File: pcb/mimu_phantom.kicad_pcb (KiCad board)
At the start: 2 copper layers, 0 parts

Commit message: I hope this did not break everything
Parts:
- added C1: 0.1uF, Capacitor_SMD:C_0805_2012Metric_Pad1.15x1.40mm_HandSolder, F.Cu at (148.8, 97.5)
- added C2: 0.1uF, Capacitor_SMD:C_0805_2012Metric_Pad1.15x1.40mm_HandSolder, F.Cu at (148.8, 100.5)
- added C3: 1uF, Capacitor_THT:C_Rect_L7.0mm_W3.5mm_P2.50mm_P5.00mm, F.Cu at (186.1, 112.7)
- added C4: 1uF, Capacitor_THT:C_Rect_L7.0mm_W3.5mm_P2.50mm_P5.00mm, F.Cu at (186.1, 117.8)
- added C_B1: 100nF, Capacitor_SMD:C_1206_3216Metric_Pad1.42x1.75mm_HandSolder, F.Cu at (181.3, 101.2)
- added C_IN1: 10uF, Capacitor_SMD:C_1206_3216Metric_Pad1.42x1.75mm_HandSolder, F.Cu at (182.7, 96.9)
- added C_IN2: 10uF, Capacitor_SMD:C_1206_3216Metric_Pad1.42x1.75mm_HandSolder, F.Cu at (190.8, 92.3)
- added C_out1: 10uF, Capacitor_SMD:C_1206_3216Metric_Pad1.42x1.75mm_HandSolder, F.Cu at (188.7, 96.9)
- added C_out2: 10uF, Capacitor_SMD:C_1206_3216Metric_Pad1.42x1.75mm_HandSolder, F.Cu at (187.2, 100.2)
- added D1: B1100, Diode_SMD:D_SMA, F.Cu at (174.3, 101.8)
- added D_B1: 1N4148, Diode_SMD:D_SMA, F.Cu at (183.8, 93.0)
- added D_LED1: LED, LED_THT:LED_D3.0mm, F.Cu at (142.2, 98.8)
- added INPUT1: XLR3, Connector_PinHeader_2.54mm:PinHeader_1x03_P2.54mm_Vertical, F.Cu at (155.4, 82.0)
- added ISP1: AVR-ISP-6, Connector_PinHeader_2.54mm:PinHeader_2x03_P2.54mm_Vertical, F.Cu at (160.1, 82.0)
- added J1: OPT, Connector_PinHeader_1.27mm:PinHeader_1x05_P1.27mm_Vertical, F.Cu at (158.0, 91.1)
- added L1: 15uH, Inductor_SMD:L_7.3x7.3_H4.5, F.Cu at (175.0, 95.1)
- added OUTPUT1: XLR3, Connector_PinHeader_2.54mm:PinHeader_1x03_P2.54mm_Vertical, F.Cu at (153.6, 92.8)
- added R1: 165R, Resistor_SMD:R_1206_3216Metric_Pad1.42x1.75mm_HandSolder, F.Cu at (143.8, 88.5)
- added R2: 110R, Resistor_SMD:R_1206_3216Metric_Pad1.42x1.75mm_HandSolder, F.Cu at (142.1, 94.0)
- added RV1: 1K_POT, Potentiometer_THT:Potentiometer_Bourns_PTV09A-2_Single_Horizontal, F.Cu at (161.4, 116.3)
- added R_1: 10, Resistor_SMD:R_1206_3216Metric_Pad1.42x1.75mm_HandSolder, F.Cu at (189.1, 79.4)
- added R_BOT1: 10k, Resistor_SMD:R_1206_3216Metric_Pad1.42x1.75mm_HandSolder, F.Cu at (189.1, 82.7)
- added R_TOP1: 31.2k, Resistor_SMD:R_1206_3216Metric_Pad1.42x1.75mm_HandSolder, F.Cu at (195.1, 79.4)
- added SENS1: Sens, Connector_PinHeader_2.54mm:PinHeader_1x04_P2.54mm_Horizontal, F.Cu at (131.2, 82.0)
- added SW2: SW_DPDT_x2, Jumper:SolderJumper-3_P1.3mm_Bridged12_RoundedPad1.0x1.5mm, F.Cu at (167.8, 81.5)
- added U1: AQY211EH, custom:DIP-4_bubble_W7.62mm, F.Cu at (143.9, 81.8)
- added U2: ATTINY88AU, Package_QFP:TQFP-32_7x7mm_P0.8mm, F.Cu at (134.7, 97.8)
- added U3: MCP16331CH, Package_TO_SOT_SMD:SOT-23-6, F.Cu at (178.1, 82.0)

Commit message: Quick layout test
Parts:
- removed R_1: 10, Resistor_SMD:R_1206_3216Metric_Pad1.42x1.75mm_HandSolder
- added R3: 6.8Ohm 0.1%, Resistor_SMD:R_1206_3216Metric_Pad1.42x1.75mm_HandSolder, F.Cu at (131.4, 88.2)
- added R4: 6.8Ohm 0.1%, Resistor_SMD:R_1206_3216Metric_Pad1.42x1.75mm_HandSolder, F.Cu at (134.0, 88.2)
- moved R_TOP1 90.3 mm to (106.0, 94.2), turned to 90 degrees
- moved R_BOT1 83.4 mm to (106.0, 89.2), turned to 90 degrees
- moved C_out1 80.3 mm to (108.4, 94.3), turned to 90 degrees
- moved C_out2 72.9 mm to (114.6, 94.3), turned to 90 degrees
- moved D_B1 72.3 mm to (111.5, 93.2), turned to 270 degrees
- moved C4 70.3 mm to (129.4, 76.2)
- moved RV1 65.8 mm to (110.4, 74.7), turned to 90 degrees
- moved C3 65.4 mm to (129.4, 80.2)
- moved U3 60.5 mm to (119.0, 94.9)
- moved C_B1 58.1 mm to (123.7, 94.2), turned to 180 degrees
- moved C_IN2 54.4 mm to (136.4, 91.2), turned to 270 degrees
- moved L1 53.6 mm to (121.8, 89.0)
- moved C_IN1 50.2 mm to (132.7, 92.6)
- moved D1 49.8 mm to (124.7, 97.4), turned to 180 degrees
- moved SW2 41.5 mm to (126.4, 78.4), turned to 90 degrees
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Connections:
- net Net-(C3-Pad1) renamed XLR_HOT
- net Net-(INPUT1-Pad3) renamed XLR_COLD
- C1 pad 2: GND -> XLR_GND
- C2 pad 2: GND -> XLR_GND
- C_IN1 pad 2: GND -> XLR_GND
- C_IN2 pad 2: GND -> XLR_GND
- C_out1 pad 2: GND -> XLR_GND
- C_out2 pad 2: GND -> XLR_GND
- D1 pad 2: GND -> XLR_GND
- D_LED1 pad 1: GND -> XLR_GND
- INPUT1 pad 1: Net-(INPUT1-Pad1) -> XLR_GND
- ISP1 pad 6: GND -> XLR_GND
- J1 pad 4: GND -> XLR_GND
- OUTPUT1 pad 1: Net-(INPUT1-Pad1) -> XLR_GND
- RV1 pad 1: GND -> XLR_GND
- R_BOT1 pad 2: GND -> XLR_GND
- R_TOP1 pad 1: Net-(R_1-Pad2) -> VCC
- SENS1 pad 2: GND -> XLR_GND
- U1 pad 2: GND -> XLR_GND
- U2 pad 21: GND -> XLR_GND
- U2 pad 5: GND -> XLR_GND
- U3 pad 2: GND -> XLR_GND
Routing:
- net XLR_GND: track 0.00 -> 159.9 mm, vias 0 -> 3
- net VCC: track 0.00 -> 135.8 mm, vias 0 -> 4
- net POT: track 0.00 -> 44.1 mm
- net XLR_COLD: track 0.00 -> 31.7 mm
- net XLR_HOT: track 0.00 -> 25.2 mm
- net Net-(C_B1-Pad1): track 0.00 -> 25.0 mm, vias 0 -> 2
- net Net-(R2-Pad2): track 0.00 -> 24.5 mm, vias 0 -> 1
- net Net-(ISP1-Pad5): track 0.00 -> 24.1 mm, vias 0 -> 2
- net Net-(J1-Pad3): track 0.00 -> 22.2 mm, vias 0 -> 2
- net +BATT: track 0.00 -> 21.1 mm, vias 0 -> 2
- net LED: track 0.00 -> 20.5 mm, vias 0 -> 2
- net Net-(J1-Pad2): track 0.00 -> 19.8 mm, vias 0 -> 2
- net Net-(R_BOT1-Pad1): track 0.00 -> 15.8 mm, vias 0 -> 2
- net Net-(J1-Pad1): track 0.00 -> 15.3 mm, vias 0 -> 1
- net SCL: track 0.00 -> 14.4 mm, vias 0 -> 1
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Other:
- board outline added: 60 x 30 mm

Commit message: Now it just has to work, lol
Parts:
- added TP1: TestPoint, Measurement_Points:Measurement_Point_Round-SMD-Pad_Small, F.Cu at (128.8, 89.8)
- added TP3: TestPoint, Measurement_Points:Measurement_Point_Round-SMD-Pad_Small, F.Cu at (103.0, 97.5)
- added TP4: TestPoint, Measurement_Points:Measurement_Point_Round-SMD-Pad_Small, F.Cu at (106.0, 85.2)
- added TP5: TestPoint, Measurement_Points:Measurement_Point_Round-SMD-Pad_Small, F.Cu at (141.0, 71.5)
- moved R3 0.31 mm to (131.4, 88.5)
- moved R4 0.30 mm to (134.0, 88.5)
- moved OUTPUT1 0.30 mm to (129.0, 72.2)
- moved D_LED1 0.10 mm to (157.4, 96.0)
- renumbered C_out1 to Cout1, C_out2 to Cout2
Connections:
- ISP1 pad 2: (no net) -> +3V0
- U2 pad 1: (no net) -> Net-(U2-Pad1)
- U2 pad 10: (no net) -> Net-(U2-Pad10)
- U2 pad 11: (no net) -> Net-(U2-Pad11)
- U2 pad 12: (no net) -> Net-(U2-Pad12)
- U2 pad 13: (no net) -> Net-(U2-Pad13)
- U2 pad 14: (no net) -> Net-(U2-Pad14)
- U2 pad 19: (no net) -> Net-(U2-Pad19)
- U2 pad 2: (no net) -> Net-(U2-Pad2)
- U2 pad 20: (no net) -> Net-(U2-Pad20)
- U2 pad 22: (no net) -> Net-(U2-Pad22)
- U2 pad 26: (no net) -> Net-(U2-Pad26)
- U2 pad 3: (no net) -> Net-(U2-Pad3)
- U2 pad 6: (no net) -> Net-(U2-Pad6)
- U2 pad 7: (no net) -> Net-(U2-Pad7)
- U2 pad 8: (no net) -> Net-(U2-Pad8)
- U2 pad 9: (no net) -> Net-(U2-Pad9)
- U3 pad 4: (no net) -> Net-(U3-Pad4)
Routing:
- net XLR_GND: track 159.9 -> 132.7 mm, vias 3 -> 8
- net VCC: track 135.8 -> 160.9 mm
- net Net-(R_BOT1-Pad1): track 15.8 -> 23.1 mm
- net +BATT: track 21.1 -> 23.9 mm
- net XLR_HOT: track 25.2 -> 27.7 mm
- net Net-(C3-Pad2): track 14.2 -> 16.7 mm
- net POT: track 44.1 -> 46.3 mm
- net SDA: track 14.2 -> 16.0 mm
- net Net-(C_B1-Pad2): track 13.6 -> 14.6 mm
- net XLR_COLD: track 31.7 -> 32.5 mm
- added copper zone on B.Cu, net XLR_GND

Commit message: Dey see me layoutin', dey hatin'
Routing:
- net LED: track 20.5 -> 21.1 mm
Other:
- board text added: "GND"
- board text added: "JLCJLCJLCJLC"
- board text added: "MIMU Phantom v0.1 PP 03.20"
- board text added: "PD0"
- board text added: "PD1"
- board text added: "PD2"
- board text added: "POT"
- board text added: "SCL"
- board text added: "SDA"
- board text added: "VCC"
- board text added: "XLR"

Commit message: Buy all the shit
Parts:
- removed Cout1: 10uF, Capacitor_SMD:C_1206_3216Metric_Pad1.42x1.75mm_HandSolder
- added C5: 0.1uF, Capacitors_THT:CP_Radial_D4.0mm_P2.00mm, F.Cu at (134.8, 90.2)
- added C6: 0.1uF, Capacitors_THT:CP_Radial_D4.0mm_P2.00mm, F.Cu at (132.0, 90.2)
- added C_out1: 10uF, Capacitor_SMD:C_1206_3216Metric_Pad1.42x1.75mm_HandSolder, F.Cu at (108.2, 94.5)
- C4: value 1uF -> 0.1uF; footprint Capacitor_THT:C_Rect_L7.0mm_W3.5mm_P2.50mm_P5.00mm -> Capacitors_THT:CP_Radial_D4.0mm_P2.00mm
- D_B1: footprint Diode_SMD:D_SMA -> Diodes_SMD:D_SOD-323_HandSoldering
- L1: footprint Inductor_SMD:L_7.3x7.3_H4.5 -> Inductors_SMD:L_7.3x7.3_H4.5
- R3, R4: footprint Resistor_SMD:R_1206_3216Metric_Pad1.42x1.75mm_HandSolder -> Resistors_THT:R_Axial_DIN0207_L6.3mm_D2.5mm_P7.62mm_Horizontal
- moved C4 19.5 mm to (134.8, 95.0)
- moved C_B1 13.9 mm to (110.6, 89.4), turned to 90 degrees
- moved R3 12.1 mm to (138.4, 78.6)
- moved TP1 11.3 mm to (140.0, 88.4)
- moved C_IN2 9.17 mm to (128.2, 95.3)
- moved R4 7.25 mm to (127.8, 84.8), turned to 0 degrees
- moved TP4 7.16 mm to (103.6, 92.0)
- moved C_IN1 7.04 mm to (125.8, 91.5), turned to 90 degrees
- moved U1 3.65 mm to (120.0, 79.8)
- moved C3 3.47 mm to (129.8, 76.8)
- moved INPUT1 3.00 mm to (129.0, 81.0)
- moved L1 2.40 mm to (119.4, 89.0)
- moved D1 2.02 mm to (123.2, 96.0)
- moved D_B1 1.84 mm to (110.6, 94.8)
- moved C_out2 1.77 mm to (112.8, 94.5)
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- renumbered Cout2 to C_out2
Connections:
- C4 pad 1: XLR_HOT -> +BATT
- C4 pad 2: Net-(C3-Pad2) -> XLR_GND
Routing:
- net XLR_GND: track 132.7 -> 88.7 mm, vias 8 -> 15
- net +BATT: track 23.9 -> 39.6 mm
- net Net-(C_B1-Pad1): track 25.0 -> 10.5 mm
- net Net-(C_B1-Pad2): track 14.6 -> 26.9 mm
- net Net-(C3-Pad2): track 16.7 -> 9.19 mm, vias 1 -> 0
- net XLR_HOT: track 27.7 -> 22.1 mm
- net Net-(R_BOT1-Pad1): track 23.1 -> 19.4 mm
- net VCC: track 160.9 -> 163.5 mm
- net Net-(SW2-Pad2): track 4.80 -> 6.94 mm
- net XLR_COLD: track 32.5 -> 33.6 mm
- net Net-(R2-Pad2): track 24.5 -> 24.2 mm, vias 1 -> 0
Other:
- board text added: "REF"

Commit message: Quick order of some pcbs
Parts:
- moved TP5 3.50 mm to (138.2, 73.6)
- moved ISP1 2.28 mm to (158.2, 74.3)
- moved J1 1.23 mm to (147.4, 97.0)
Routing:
- net XLR_GND: track 88.7 -> 82.3 mm
- net VCC: track 163.5 -> 168.9 mm, vias 4 -> 5
- net Net-(ISP1-Pad4): track 11.2 -> 7.63 mm
- net Net-(J1-Pad1): track 15.8 -> 14.4 mm, vias 1 -> 2
- net Net-(J1-Pad3): track 22.5 -> 21.2 mm
- net Net-(J1-Pad2): track 19.7 -> 18.5 mm
- net Net-(ISP1-Pad3): track 9.67 -> 8.92 mm
- net Net-(ISP1-Pad5): track 24.2 -> 23.5 mm, vias 2 -> 1
- net POT: track 46.3 -> 45.7 mm
- net Net-(ISP1-Pad1): track 12.0 -> 11.5 mm, vias 2 -> 1
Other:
- board text added: "- - wow, much space - -"
- board text added: "MIMU Phantom v0.2 PP 03.20"
- board text added: "MISO"
- board text added: "MOSI"
- board text added: "RST"
- board text added: "SCK"
- board text removed: "MIMU Phantom v0.1 PP 03.20"

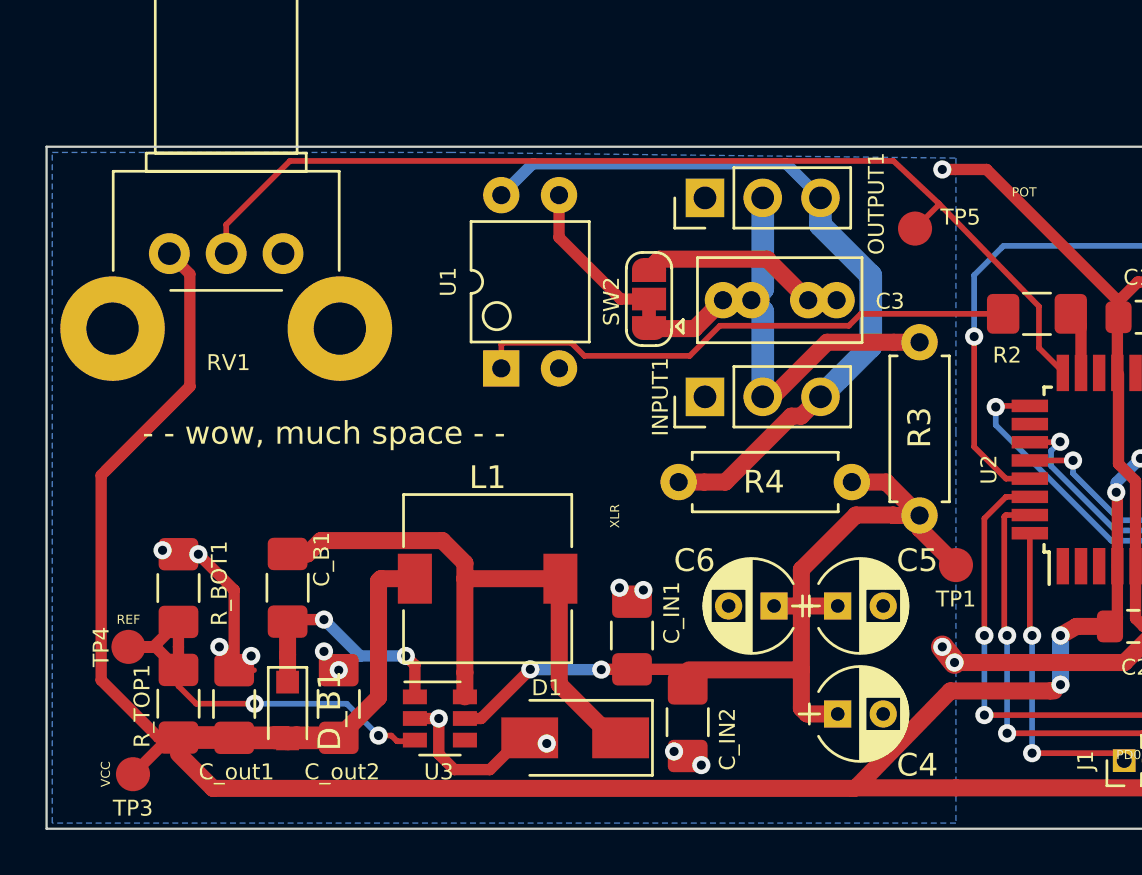
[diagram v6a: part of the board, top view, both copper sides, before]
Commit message: Cap not needed for XLR
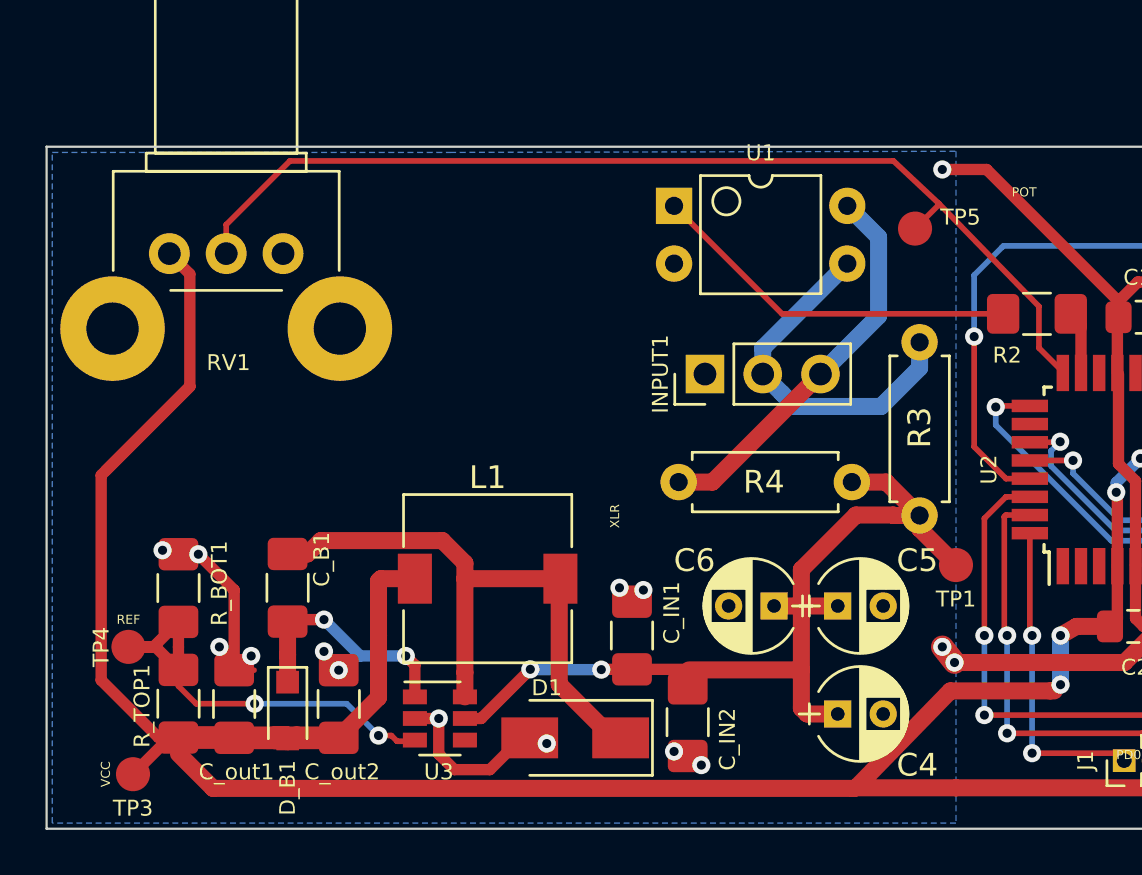
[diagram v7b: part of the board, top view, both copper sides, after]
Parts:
- removed C3: 1uF, Capacitor_THT:C_Rect_L7.0mm_W3.5mm_P2.50mm_P5.00mm
- removed OUTPUT1: XLR3, Connector_PinHeader_2.54mm:PinHeader_1x03_P2.54mm_Vertical
- removed SW2: SW_DPDT_x2, Jumper:SolderJumper-3_P1.3mm_Bridged12_RoundedPad1.0x1.5mm
- R1: value 165R -> 333R
- R2: value 110R -> 1k
- moved U1 10.4 mm to (127.6, 72.6), turned to 0 degrees
- moved INPUT1 1.00 mm to (129.0, 80.0)
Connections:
- U1 pad 3: Net-(SW2-Pad2) -> XLR_HOT
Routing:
- net XLR_COLD: track 33.6 -> 17.2 mm
- net Net-(C3-Pad2): track 9.19 -> 0.00 mm
- net Net-(R2-Pad2): track 24.2 -> 16.4 mm
- net Net-(SW2-Pad2): track 6.94 -> 0.00 mm
- net XLR_HOT: track 22.1 -> 15.7 mm
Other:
- board text added: "https://github.com/Cirromulus/mimu"
- board text removed: "- - wow, much space - -"

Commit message: Something new about the PCB?
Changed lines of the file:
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@@
   )
   (setup
-    (last_trace_width 0.75)
+    (last_trace_width 0.25)
     (user_trace_width 0.25)
     (user_trace_width 0.5)
@@
     (descr "4-lead though-hole mounted DIP package, row spacing 7.62 mm (300 mils)")
     (tags "THT DIP DIL PDIP 2.54mm 7.62mm 300mil")
-    (fp_text reference U1 (at 3.81 -2.33) (layer F.SilkS)
-      (effects (font (size 0.7 0.7) (thickness 0.15)))
-    )
+    (fp_text reference U1 (at 3.8 1.2) (layer F.SilkS)
+      (effects (font (size 0.7 0.7) (thickness 0.15)))
+    )
